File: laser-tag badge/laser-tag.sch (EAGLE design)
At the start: 46 parts, among them J1 JUMPER_SOLDER_1X2_CLOSED, J2 JUMPER_SOLDER_1X2_OPEN, J3 JUMPER_SOLDER_1X2_CLOSED, J4 JUMPER_SOLDER_1X2_CLOSED, J5 JUMPER_SOLDER_1X2_CLOSED, P1 E1260CS021, Q1 BSS123, Q2 BSS123, U1 MKL27Z256VLH4

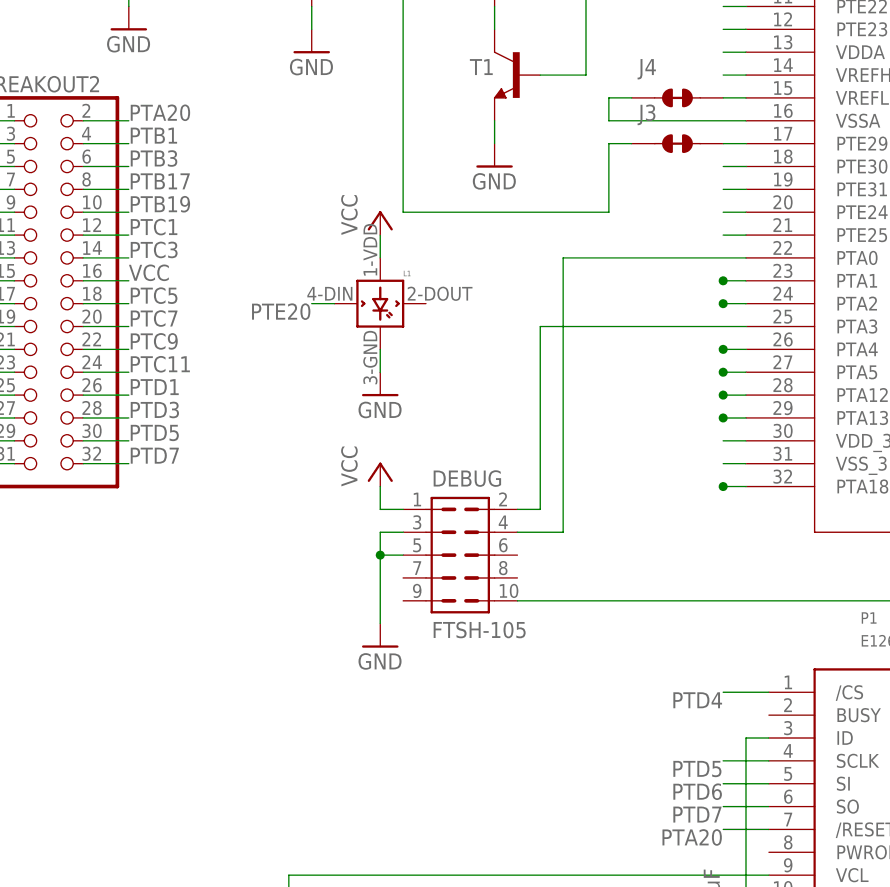
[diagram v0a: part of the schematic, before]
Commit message: Add buzzer
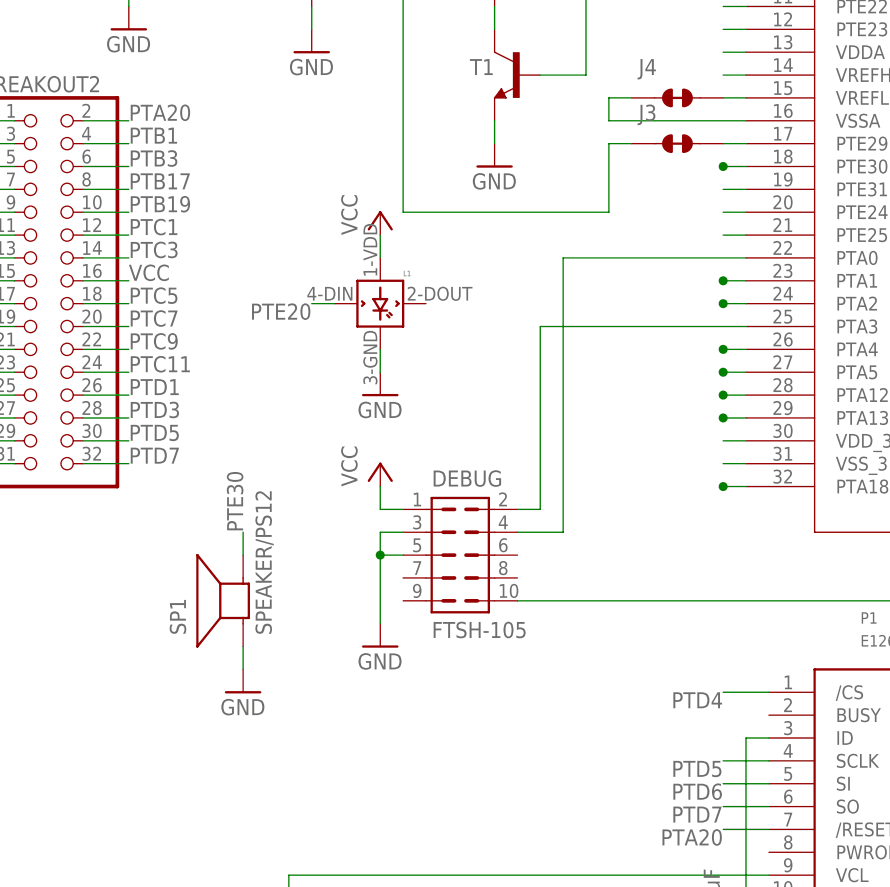
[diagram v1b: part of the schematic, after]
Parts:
- added SP1: SPEAKER/PS12, adafruit:SPEAKER/PS12
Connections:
- net GND: now also SP1.+
- net PTE30: now also SP1.-
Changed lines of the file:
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@@
 <part name="P+7" library="supply1" deviceset="VCC" device=""/>
 <part name="J5" library="Jumpers" deviceset="JUMPER_SOLDER_1X2_CLOSED" device=""/>
+<part name="SP1" library="adafruit" deviceset="SPEAKER" device="/PS12"/>
+<part name="GND9" library="supply1" deviceset="GND" device=""/>
 </parts>
 <sheets>
@@
 <instance part="P+7" gate="VCC" x="-30.48" y="50.8"/>
 <instance part="J5" gate="J" x="2.54" y="99.06"/>
+<instance part="SP1" gate="S1" x="-45.72" y="7.62" rot="R90"/>
+<instance part="GND9" gate="1" x="-45.72" y="-2.54"/>
 </instances>
 <busses>
@@
 <wire x1="-17.78" y1="58.42" x2="-17.78" y2="60.96" width="0.1524" layer="91"/>
 </segment>
+<segment>
+<pinref part="GND9" gate="1" pin="GND"/>
+<pinref part="SP1" gate="S1" pin="+"/>
+<wire x1="-45.72" y1="0" x2="-45.72" y2="2.54" width="0.1524" layer="91"/>
+</segment>
 </net>
 <net name="VCC" class="0">
@@
 <pinref part="U1" gate="A" pin="PTE30"/>
 <wire x1="10.16" y1="55.88" x2="7.62" y2="55.88" width="0.1524" layer="91"/>
-</segment>
-</net>
+<junction x="7.62" y="55.88"/>
+</segment>
+<segment>
+<pinref part="SP1" gate="S1" pin="-"/>
+<wire x1="-45.72" y1="12.7" x2="-45.72" y2="15.24" width="0.1524" layer="91"/>
+<label x="-45.72" y="15.24" size="1.778" layer="95" rot="R90"/>
+</segment>
+</net>

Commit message: Finishing up the layout
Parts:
- removed DEBUG: FTSH-105, Samtec:FTSH-105-01-XXX-DV-K
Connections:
- new net N$11: J3.1, PD1.A, PD2.A, R1.2
- net GND: no longer DEBUG.3, DEBUG.5
- net PTA0: no longer DEBUG.4
- net PTA20: no longer DEBUG.10
- net PTA3: no longer DEBUG.2
- net PTE29: no longer J3.1, PD1.A, PD2.A, R1.2
- net VCC: no longer DEBUG.1
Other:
- note added: "RESET"
- note added: "SWD_CLK"
- note added: "SWD_DIO"

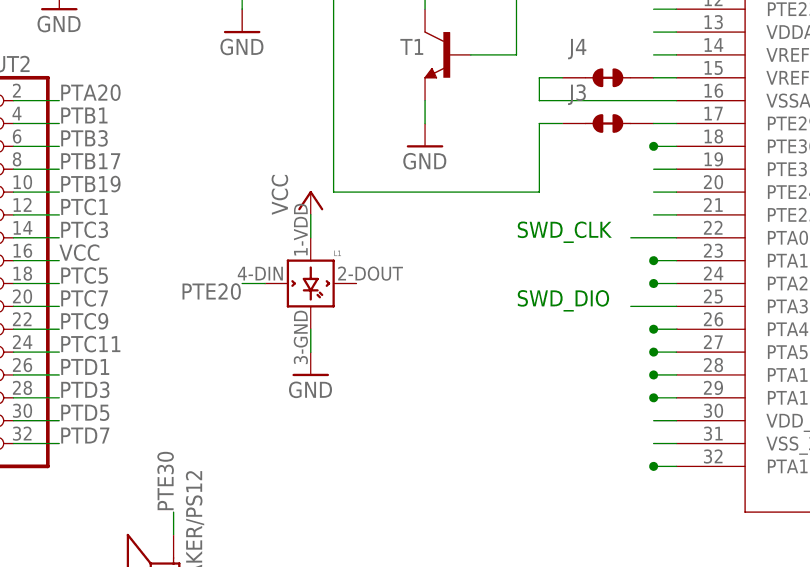
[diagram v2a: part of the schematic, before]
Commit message: Add a bypass cap for the LED
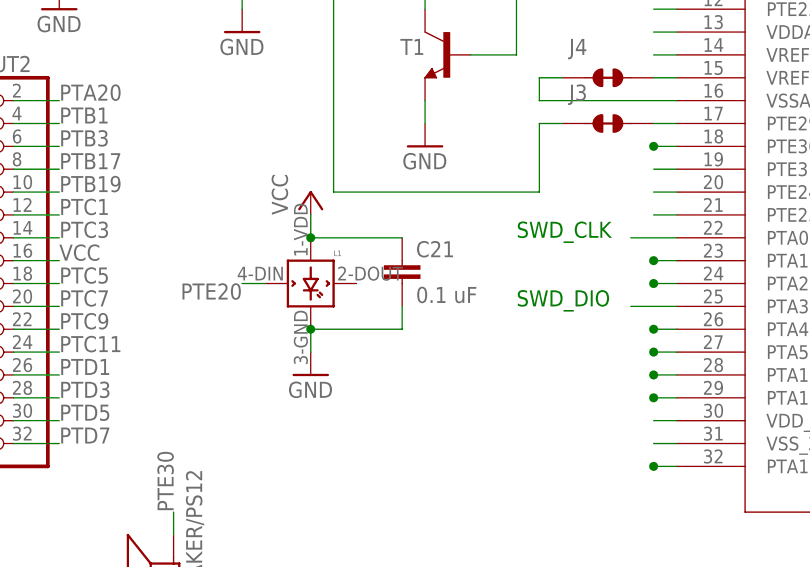
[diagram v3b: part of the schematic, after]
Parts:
- added C21: 0.1 uF, rcl:C-EUC0603K
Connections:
- net GND: now also C21.2
- net VCC: now also C21.1
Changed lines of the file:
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@@
 <part name="SP1" library="adafruit" deviceset="SPEAKER" device="/PS12"/>
 <part name="GND9" library="supply1" deviceset="GND" device=""/>
+<part name="C21" library="rcl" deviceset="C-EU" device="C0603K" value="0.1 uF"/>
 </parts>
 <sheets>
@@
 <instance part="SP1" gate="S1" x="-45.72" y="7.62" rot="R90"/>
 <instance part="GND9" gate="1" x="-45.72" y="-2.54"/>
+<instance part="C21" gate="G$1" x="-20.32" y="43.18"/>
 </instances>
 <busses>
@@
 <pinref part="GND7" gate="1" pin="GND"/>
 <wire x1="-30.48" y1="35.56" x2="-30.48" y2="33.02" width="0.1524" layer="91"/>
+<pinref part="C21" gate="G$1" pin="2"/>
+<wire x1="-30.48" y1="35.56" x2="-20.32" y2="35.56" width="0.1524" layer="91"/>
+<wire x1="-20.32" y1="35.56" x2="-20.32" y2="38.1" width="0.1524" layer="91"/>
+<junction x="-30.48" y="35.56"/>
 </segment>
 <segment>
@@
 <pinref part="L1" gate="G$1" pin="VDD"/>
 <wire x1="-30.48" y1="48.26" x2="-30.48" y2="45.72" width="0.1524" layer="91"/>
+<pinref part="C21" gate="G$1" pin="1"/>
+<wire x1="-20.32" y1="45.72" x2="-30.48" y2="45.72" width="0.1524" layer="91"/>
+<junction x="-30.48" y="45.72"/>
 </segment>
 </net>

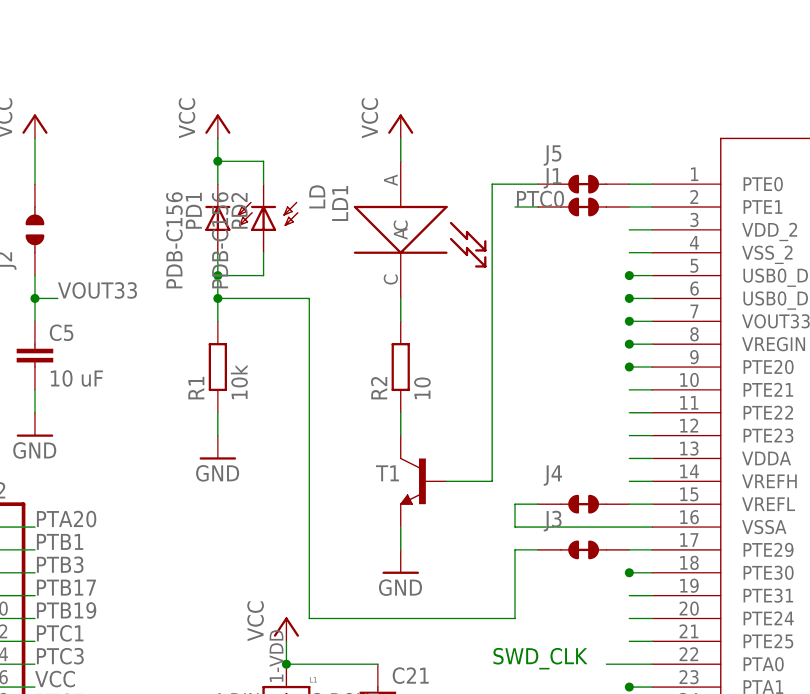
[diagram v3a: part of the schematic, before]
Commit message: Add pulldown for T1 gate
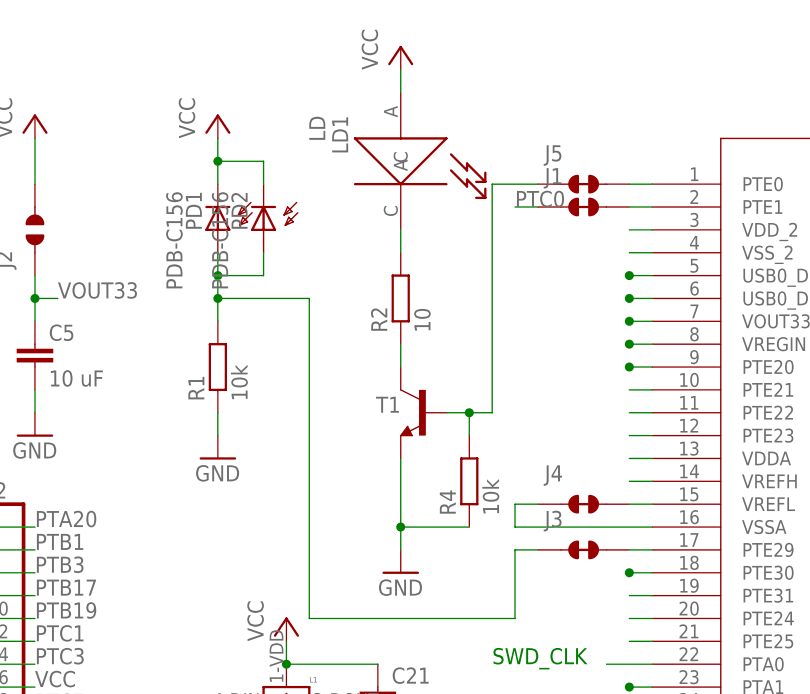
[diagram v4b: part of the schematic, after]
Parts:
- added R4: 10k, rcl:R-EU_R0603
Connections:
- net GND: now also R4.1
- net N$10: now also R4.2
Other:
- moved on the sheet: LD1, R2, T1
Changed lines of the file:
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@@
 <part name="GND9" library="supply1" deviceset="GND" device=""/>
 <part name="C21" library="rcl" deviceset="C-EU" device="C0603K" value="0.1 uF"/>
+<part name="R4" library="rcl" deviceset="R-EU_" device="R0603" value="10k"/>
 </parts>
 <sheets>
@@
 <instance part="BREAKOUT1" gate="A" x="-109.22" y="43.18"/>
 <instance part="BREAKOUT2" gate="A" x="-68.58" y="43.18"/>
-<instance part="LD1" gate="A" x="-17.78" y="93.98" rot="R270"/>
-<instance part="P+1" gate="VCC" x="-17.78" y="106.68"/>
-<instance part="T1" gate="G$1" x="-15.24" y="66.04" smashed="yes" rot="MR0">
-<attribute name="NAME" x="-17.78" y="66.04" size="1.778" layer="95" rot="MR0"/>
-<attribute name="VALUE" x="-5.08" y="71.12" size="1.778" layer="96" rot="MR0"/>
+<instance part="LD1" gate="A" x="-17.78" y="101.6" rot="R270"/>
+<instance part="P+1" gate="VCC" x="-17.78" y="114.3"/>
+<instance part="T1" gate="G$1" x="-15.24" y="73.66" smashed="yes" rot="MR0">
+<attribute name="NAME" x="-17.78" y="73.66" size="1.778" layer="95" rot="MR0"/>
+<attribute name="VALUE" x="-5.08" y="78.74" size="1.778" layer="96" rot="MR0"/>
 </instance>
 <instance part="GND1" gate="1" x="-17.78" y="55.88"/>
@@
 <instance part="GND2" gate="1" x="-38.1" y="68.58"/>
 <instance part="USB" gate="G$1" x="-106.68" y="5.08"/>
-<instance part="R2" gate="G$1" x="-17.78" y="78.74" rot="R90"/>
+<instance part="R2" gate="G$1" x="-17.78" y="86.36" rot="R90"/>
 <instance part="C5" gate="G$1" x="-58.42" y="81.28"/>
 <instance part="GND5" gate="1" x="-58.42" y="71.12"/>
@@
 <instance part="GND9" gate="1" x="-45.72" y="-2.54"/>
 <instance part="C21" gate="G$1" x="-20.32" y="43.18"/>
+<instance part="R4" gate="G$1" x="-10.16" y="66.04" rot="R90"/>
 </instances>
 <busses>
@@
 <pinref part="T1" gate="G$1" pin="E"/>
 <wire x1="-17.78" y1="58.42" x2="-17.78" y2="60.96" width="0.1524" layer="91"/>
+<pinref part="R4" gate="G$1" pin="1"/>
+<wire x1="-17.78" y1="60.96" x2="-17.78" y2="68.58" width="0.1524" layer="91"/>
+<wire x1="-10.16" y1="60.96" x2="-17.78" y2="60.96" width="0.1524" layer="91"/>
+<junction x="-17.78" y="60.96"/>
 </segment>
 <segment>
@@
 <pinref part="P+1" gate="VCC" pin="VCC"/>
 <pinref part="LD1" gate="A" pin="A"/>
-<wire x1="-17.78" y1="104.14" x2="-17.78" y2="101.6" width="0.1524" layer="91"/>
+<wire x1="-17.78" y1="111.76" x2="-17.78" y2="109.22" width="0.1524" layer="91"/>
 </segment>
 <segment>
@@
 <pinref part="T1" gate="G$1" pin="C"/>
 <pinref part="R2" gate="G$1" pin="1"/>
-<wire x1="-17.78" y1="71.12" x2="-17.78" y2="73.66" width="0.1524" layer="91"/>
+<wire x1="-17.78" y1="78.74" x2="-17.78" y2="81.28" width="0.1524" layer="91"/>
 </segment>
 </net>
@@
 <pinref part="R2" gate="G$1" pin="2"/>
 <pinref part="LD1" gate="A" pin="C"/>
-<wire x1="-17.78" y1="83.82" x2="-17.78" y2="86.36" width="0.1524" layer="91"/>
+<wire x1="-17.78" y1="91.44" x2="-17.78" y2="93.98" width="0.1524" layer="91"/>
 </segment>
 </net>
@@
 <segment>
 <pinref part="T1" gate="G$1" pin="B"/>
-<wire x1="-12.7" y1="66.04" x2="-7.62" y2="66.04" width="0.1524" layer="91"/>
-<wire x1="-7.62" y1="66.04" x2="-7.62" y2="99.06" width="0.1524" layer="91"/>
+<wire x1="-12.7" y1="73.66" x2="-10.16" y2="73.66" width="0.1524" layer="91"/>
+<wire x1="-10.16" y1="73.66" x2="-7.62" y2="73.66" width="0.1524" layer="91"/>
+<wire x1="-7.62" y1="73.66" x2="-7.62" y2="99.06" width="0.1524" layer="91"/>
 <pinref part="J5" gate="J" pin="1"/>
 <wire x1="-7.62" y1="99.06" x2="-2.54" y2="99.06" width="0.1524" layer="91"/>
-</segment>
-</net>
+<pinref part="R4" gate="G$1" pin="2"/>
+<wire x1="-10.16" y1="71.12" x2="-10.16" y2="73.66" width="0.1524" layer="91"/>
+<junction x="-10.16" y="73.66"/>
+</segment>
+</net>

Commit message: Second battery for more power
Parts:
- added BAT2: BK-883, adafruit:CR2032SMT
- renumbered BAT to BAT1
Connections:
- net GND: now also BAT2.-
- net VCC: now also BAT2.+, BAT2.+1
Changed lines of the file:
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@@
 <parts>
 <part name="U1" library="Freescale" deviceset="MKL27Z256VLH4" device=""/>
-<part name="BAT" library="adafruit" deviceset="CR2032" device="SMT" value="BK-883"/>
+<part name="BAT1" library="adafruit" deviceset="CR2032" device="SMT" value="BK-883"/>
 <part name="P+3" library="supply1" deviceset="VCC" device=""/>
 <part name="GND3" library="supply1" deviceset="GND" device=""/>
@@
 <part name="C21" library="rcl" deviceset="C-EU" device="C0603K" value="0.1 uF"/>
 <part name="R4" library="rcl" deviceset="R-EU_" device="R0603" value="10k"/>
+<part name="BAT2" library="adafruit" deviceset="CR2032" device="SMT" value="BK-883"/>
 </parts>
 <sheets>
@@
 <instances>
 <instance part="U1" gate="A" x="10.16" y="99.06"/>
-<instance part="BAT" gate="G$1" x="-114.3" y="88.9" rot="R90"/>
+<instance part="BAT1" gate="G$1" x="-114.3" y="88.9" rot="R90"/>
 <instance part="P+3" gate="VCC" x="-101.6" y="104.14"/>
 <instance part="GND3" gate="1" x="-114.3" y="76.2"/>
@@
 <instance part="C21" gate="G$1" x="-20.32" y="43.18"/>
 <instance part="R4" gate="G$1" x="-10.16" y="66.04" rot="R90"/>
+<instance part="BAT2" gate="G$1" x="-124.46" y="88.9" rot="R90"/>
 </instances>
 <busses>
@@
 <net name="GND" class="0">
 <segment>
-<pinref part="BAT" gate="G$1" pin="-"/>
+<pinref part="BAT1" gate="G$1" pin="-"/>
 <pinref part="GND3" gate="1" pin="GND"/>
 <wire x1="-114.3" y1="83.82" x2="-114.3" y2="81.28" width="0.1524" layer="91"/>
@@
 <wire x1="-71.12" y1="81.28" x2="-71.12" y2="86.36" width="0.1524" layer="91"/>
 <junction x="-81.28" y="81.28"/>
+<pinref part="BAT2" gate="G$1" pin="-"/>
+<wire x1="-114.3" y1="81.28" x2="-124.46" y2="81.28" width="0.1524" layer="91"/>
+<wire x1="-124.46" y1="81.28" x2="-124.46" y2="83.82" width="0.1524" layer="91"/>
 </segment>
 <segment>
@@
 <junction x="-101.6" y="96.52"/>
 <pinref part="P+3" gate="VCC" pin="VCC"/>
-<pinref part="BAT" gate="G$1" pin="+"/>
-<pinref part="BAT" gate="G$1" pin="+1"/>
+<pinref part="BAT1" gate="G$1" pin="+"/>
+<pinref part="BAT1" gate="G$1" pin="+1"/>
 <wire x1="-111.76" y1="93.98" x2="-111.76" y2="96.52" width="0.1524" layer="91"/>
 <wire x1="-111.76" y1="96.52" x2="-116.84" y2="96.52" width="0.1524" layer="91"/>
@@
 <junction x="-111.76" y="96.52"/>
 <junction x="-101.6" y="96.52"/>
-</segment>
-<segment>
+<pinref part="BAT2" gate="G$1" pin="+1"/>
+<wire x1="-121.92" y1="93.98" x2="-121.92" y2="96.52" width="0.1524" layer="91"/>
+<wire x1="-121.92" y1="96.52" x2="-116.84" y2="96.52" width="0.1524" layer="91"/>
+<junction x="-116.84" y="96.52"/>
+<pinref part="BAT2" gate="G$1" pin="+"/>
+<wire x1="-127" y1="93.98" x2="-127" y2="96.52" width="0.1524" layer="91"/>
+<wire x1="-127" y1="96.52" x2="-121.92" y2="96.52" width="0.1524" layer="91"/>
+<junction x="-121.92" y="96.52"/>
+</segment>
+<segment>

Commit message: Remove discharge FETs and use PTA19 for EPD reset
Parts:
- removed Q1, Q2: BSS123, transistor-small-signal:BSS123
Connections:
- net GND: no longer Q1.S, Q2.S
- net N$5: no longer Q1.D
- net N$7: no longer Q2.D
- net PTA19: now also P1./RESET; no longer Q1.G, Q2.G
- net PTA20: no longer P1./RESET
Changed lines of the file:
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@@
 <part name="P+6" library="supply1" deviceset="VCC" device=""/>
 <part name="D1" library="diode" deviceset="CGRM400*-G" device="" technology="1" value="NRVTS245ESFT1G"/>
-<part name="Q1" library="transistor-small-signal" deviceset="BSS123" device=""/>
-<part name="Q2" library="transistor-small-signal" deviceset="BSS123" device=""/>
 <part name="J4" library="Jumpers" deviceset="JUMPER_SOLDER_1X2_CLOSED" device=""/>
 <part name="S3" library="Switches" deviceset="TPA511GLFS" device=""/>
@@
 <instance part="P+6" gate="VCC" x="-10.16" y="-76.2"/>
 <instance part="D1" gate="G$1" x="-25.4" y="-99.06" rot="R270"/>
-<instance part="Q1" gate="G$1" x="-50.8" y="-101.6"/>
-<instance part="Q2" gate="G$1" x="-63.5" y="-101.6"/>
 <instance part="J4" gate="J" x="2.54" y="63.5"/>
 <instance part="S3" gate="G$1" x="144.78" y="63.5" rot="R180"/>
@@
 <wire x1="-25.4" y1="-101.6" x2="-25.4" y2="-114.3" width="0.1524" layer="91"/>
 <junction x="-25.4" y="-114.3"/>
-<pinref part="Q1" gate="G$1" pin="S"/>
-<wire x1="-50.8" y1="-106.68" x2="-50.8" y2="-114.3" width="0.1524" layer="91"/>
-<wire x1="-50.8" y1="-114.3" x2="-40.64" y2="-114.3" width="0.1524" layer="91"/>
-<junction x="-40.64" y="-114.3"/>
-<pinref part="Q2" gate="G$1" pin="S"/>
-<wire x1="-63.5" y1="-106.68" x2="-63.5" y2="-114.3" width="0.1524" layer="91"/>
-<wire x1="-63.5" y1="-114.3" x2="-50.8" y2="-114.3" width="0.1524" layer="91"/>
-<junction x="-50.8" y="-114.3"/>
 </segment>
 <segment>
@@
 <net name="PTA20" class="0">
 <segment>
-<pinref part="U1" gate="A" pin="PTA20"/>
-<wire x1="116.84" y1="22.86" x2="121.92" y2="22.86" width="0.1524" layer="91"/>
-</segment>
-<segment>
 <pinref part="BREAKOUT2" gate="A" pin="2"/>
 <wire x1="-63.5" y1="60.96" x2="-58.42" y2="60.96" width="0.1524" layer="91"/>
@@
 </segment>
 <segment>
-<pinref part="P1" gate="G$1" pin="/RESET"/>
-<wire x1="12.7" y1="-17.78" x2="7.62" y2="-17.78" width="0.1524" layer="91"/>
-<label x="7.62" y="-17.78" size="1.778" layer="95" rot="R180"/>
+<pinref part="U1" gate="A" pin="PTA20"/>
+<wire x1="116.84" y1="22.86" x2="121.92" y2="22.86" width="0.1524" layer="91"/>
 </segment>
 </net>
@@
 </segment>
 <segment>
-<pinref part="Q1" gate="G$1" pin="G"/>
-<wire x1="-55.88" y1="-104.14" x2="-58.42" y2="-104.14" width="0.1524" layer="91"/>
-<wire x1="-58.42" y1="-104.14" x2="-58.42" y2="-106.68" width="0.1524" layer="91"/>
-<wire x1="-58.42" y1="-106.68" x2="-71.12" y2="-106.68" width="0.1524" layer="91"/>
-<wire x1="-71.12" y1="-106.68" x2="-71.12" y2="-104.14" width="0.1524" layer="91"/>
-<pinref part="Q2" gate="G$1" pin="G"/>
-<wire x1="-71.12" y1="-104.14" x2="-68.58" y2="-104.14" width="0.1524" layer="91"/>
-<label x="-71.12" y="-104.14" size="1.778" layer="95" rot="R180"/>
+<pinref part="P1" gate="G$1" pin="/RESET"/>
+<wire x1="12.7" y1="-17.78" x2="7.62" y2="-17.78" width="0.1524" layer="91"/>
+<label x="7.62" y="-17.78" size="1.778" layer="95" rot="R180"/>
 </segment>
 </net>
@@
 <wire x1="12.7" y1="-91.44" x2="-12.7" y2="-91.44" width="0.1524" layer="91"/>
 <wire x1="-12.7" y1="-91.44" x2="-12.7" y2="-96.52" width="0.1524" layer="91"/>
-<pinref part="Q1" gate="G$1" pin="D"/>
-<wire x1="-12.7" y1="-91.44" x2="-50.8" y2="-91.44" width="0.1524" layer="91"/>
-<wire x1="-50.8" y1="-91.44" x2="-50.8" y2="-96.52" width="0.1524" layer="91"/>
-<junction x="-12.7" y="-91.44"/>
 </segment>
 </net>
@@
 <wire x1="12.7" y1="-86.36" x2="-33.02" y2="-86.36" width="0.1524" layer="91"/>
 <wire x1="-33.02" y1="-86.36" x2="-33.02" y2="-96.52" width="0.1524" layer="91"/>
-<pinref part="Q2" gate="G$1" pin="D"/>
-<wire x1="-33.02" y1="-86.36" x2="-63.5" y2="-86.36" width="0.1524" layer="91"/>
-<wire x1="-63.5" y1="-86.36" x2="-63.5" y2="-96.52" width="0.1524" layer="91"/>
-<junction x="-33.02" y="-86.36"/>
-</segment>
-</net>
+</segment>
+</net>

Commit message: Make compatible with V0 badges again
Since we don't need to control reset to fix EPD stuck problems
wire it back to PTA20 and revert the code changes.
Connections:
- net PTA19: no longer P1./RESET
- net PTA20: now also P1./RESET
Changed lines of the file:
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@@
 <net name="PTA20" class="0">
+<segment>
+<pinref part="U1" gate="A" pin="PTA20"/>
+<wire x1="116.84" y1="22.86" x2="121.92" y2="22.86" width="0.1524" layer="91"/>
+</segment>
 <segment>
 <pinref part="BREAKOUT2" gate="A" pin="2"/>
@@
 </segment>
 <segment>
-<pinref part="U1" gate="A" pin="PTA20"/>
-<wire x1="116.84" y1="22.86" x2="121.92" y2="22.86" width="0.1524" layer="91"/>
+<pinref part="P1" gate="G$1" pin="/RESET"/>
+<wire x1="12.7" y1="-17.78" x2="7.62" y2="-17.78" width="0.1524" layer="91"/>
+<label x="7.62" y="-17.78" size="1.778" layer="95" rot="R180"/>
 </segment>
 </net>
@@
 <label x="-76.2" y="60.96" size="1.778" layer="95" rot="R180"/>
 </segment>
-<segment>
-<pinref part="P1" gate="G$1" pin="/RESET"/>
-<wire x1="12.7" y1="-17.78" x2="7.62" y2="-17.78" width="0.1524" layer="91"/>
-<label x="7.62" y="-17.78" size="1.778" layer="95" rot="R180"/>
-</segment>
-</net>
+</net>
